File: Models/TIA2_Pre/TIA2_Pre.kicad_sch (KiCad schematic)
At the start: 0 parts

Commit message: Save progress
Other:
- note added: "Input: 2.5V power Input: -1.5V power Input: current Output: pre voltage Ground connection(s) not yet elaborated"
- note removed: "Input: 2.5V power (grounded interconnect) Input: -1.5V power (grounded interconnect) Input: current Output: voltage (grounded interconnect)"
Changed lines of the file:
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@@
 	(generator_version "9.0")
 	(paper "A4")
-	(text "Input: 2.5V power (grounded interconnect)\nInput: -1.5V power (grounded interconnect)\nInput: current\nOutput: voltage (grounded interconnect)"
+	(text "Input: 2.5V power\nInput: -1.5V power\nInput: current\nOutput: pre voltage\n\nGround connection(s) not yet elaborated"
 		(exclude_from_sim no)
 		(at 158.242 76.962 0)

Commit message: Save progress
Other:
- note added: "Input: 2.5V power Input: -1.5V power Input: current Output: pre voltage Output: AD8615 output Ground connection(s) not yet elaborated"
- note removed: "Input: 2.5V power Input: -1.5V power Input: current Output: pre voltage Ground connection(s) not yet elaborated"
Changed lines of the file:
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@@
 	(generator_version "9.0")
 	(paper "A4")
-	(text "Input: 2.5V power\nInput: -1.5V power\nInput: current\nOutput: pre voltage\n\nGround connection(s) not yet elaborated"
+	(text "Input: 2.5V power\nInput: -1.5V power\nInput: current\nOutput: pre voltage\nOutput: AD8615 output\n\nGround connection(s) not yet elaborated"
 		(exclude_from_sim no)
 		(at 158.242 76.962 0)

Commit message: Save progress
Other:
- note added: "Input: 2.5V power Input: -1.5V power Input: current Output: pre voltage Output: AD8615 output"
- note removed: "Input: 2.5V power Input: -1.5V power Input: current Output: pre voltage Output: AD8615 output Ground connection(s) not yet elaborated"
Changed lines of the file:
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@@
 	(generator_version "9.0")
 	(paper "A4")
-	(text "Input: 2.5V power\nInput: -1.5V power\nInput: current\nOutput: pre voltage\nOutput: AD8615 output\n\nGround connection(s) not yet elaborated"
+	(text "Input: 2.5V power\nInput: -1.5V power\nInput: current\nOutput: pre voltage\nOutput: AD8615 output"
 		(exclude_from_sim no)
 		(at 158.242 76.962 0)
@@
 	(sheet
 		(at 101.6 76.2)
-		(size 50.8 50.8)
+		(size 50.8 25.4)
 		(exclude_from_sim no)
 		(in_bom yes)
@@
 		)
 		(property "Sheetfile" "Amplifier.kicad_sch"
-			(at 101.6 127.5846 0)
+			(at 101.6 102.1846 0)
 			(effects
 				(font

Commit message: Save progress
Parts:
- added C3, C4: 1 uF, 0603, symbol Device:C
- added J3: Conn_01x03_Pin, symbol Connector:Conn_01x03_Pin
- added R1: 10, symbol Device:R_US
- added R3: 330M, 5%, 0603, symbol Device:R_US
- added U2: AD8615, symbol Amplifier_Operational:OP179GRT
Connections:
- new net: J3.1 (Pin_1), R1.1
- new net -1.5V: C4.1, U2.5 (V-)
- new net 2.5V: C3.1, U2.2 (V+)
- new net AD8615_Output: U2.1
- new net Current: R3.1, U2.4 (-)
- new net GND: C3.2, C4.2, J3.3 (Pin_3), R1.2
- new net ISO_GND: J3.2 (Pin_2), U2.3 (+)
- new net PreVoltage: R3.2
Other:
- removed sheet Amplifier
- note removed: "Input: 2.5V power Input: -1.5V power Input: current Output: pre voltage Output: AD8615 output"

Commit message: Save progress
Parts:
- R3: value 330M, 5%, 0603 -> 1G, 5%, 0603; Cost (none) -> $4.19; Purchase Link https://www.digikey.com/en/products/detail/vishay-dale/CRCW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 -> https://www.digikey.com/en/products/detail/stackpole-electr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
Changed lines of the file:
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@@
 			)
 		)
-		(property "Value" "330M, 5%, 0603"
+		(property "Value" "1G, 5%, 0603"
 			(at 135.89 95.25 90)
 			(effects
@@
 			)
 		)
-		(property "Purchase Link" "https://www.digikey.com/en/products/detail/vishay-dale/CRCW0603330MJPEAHR/5072104"
+		(property "Purchase Link" "https://www.digikey.com/en/products/detail/stackpole-electronics-inc/HVCB0603JDD1G00/5801231"
 			(at 135.89 99.06 0)
 			(effects
 				(font
+					(size 1.27 1.27)
+				)
+				(hide yes)
+			)
+		)
+		(property "Cost" "$4.19"
+			(at 135.89 99.06 90)
+			(effects
+				(font

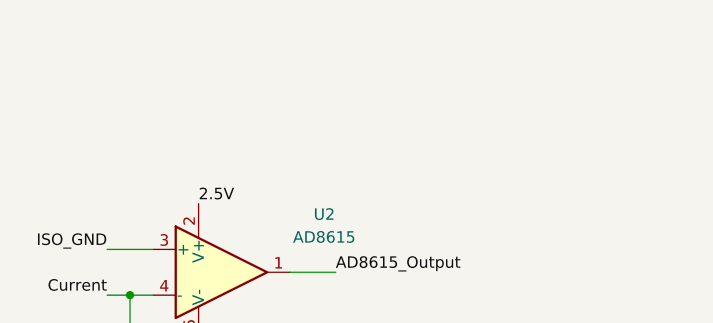
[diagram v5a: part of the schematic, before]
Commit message: Weird bug messes up FEM simulation results when I recompute objects in FreeCAD
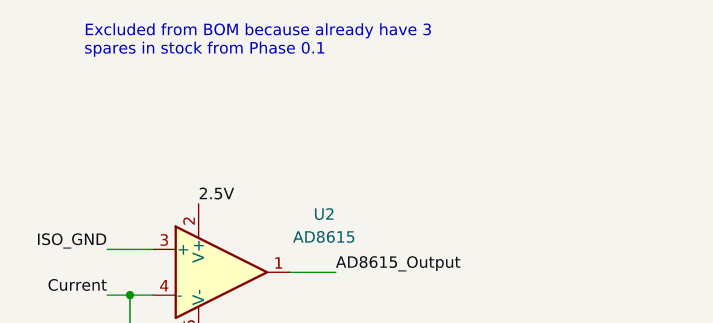
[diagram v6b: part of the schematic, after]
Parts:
- U2: now left out of the parts list
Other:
- note added: "Excluded from BOM because already have 3 spares in stock from Phase 0.1"
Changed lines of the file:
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@@
 	(generator_version "9.0")
 	(paper "A4")
+	(text "Excluded from BOM because already have 3\nspares in stock from Phase 0.1"
+		(exclude_from_sim no)
+		(at 121.92 46.228 0)
+		(effects
+			(font
+				(size 1.27 1.27)
+			)
+			(justify left top)
+		)
+	)
 	(junction
 		(at 127 76.2)
@@
 		(unit 1)
 		(exclude_from_sim no)
-		(in_bom yes)
+		(in_bom no)
 		(on_board yes)
 		(dnp no)

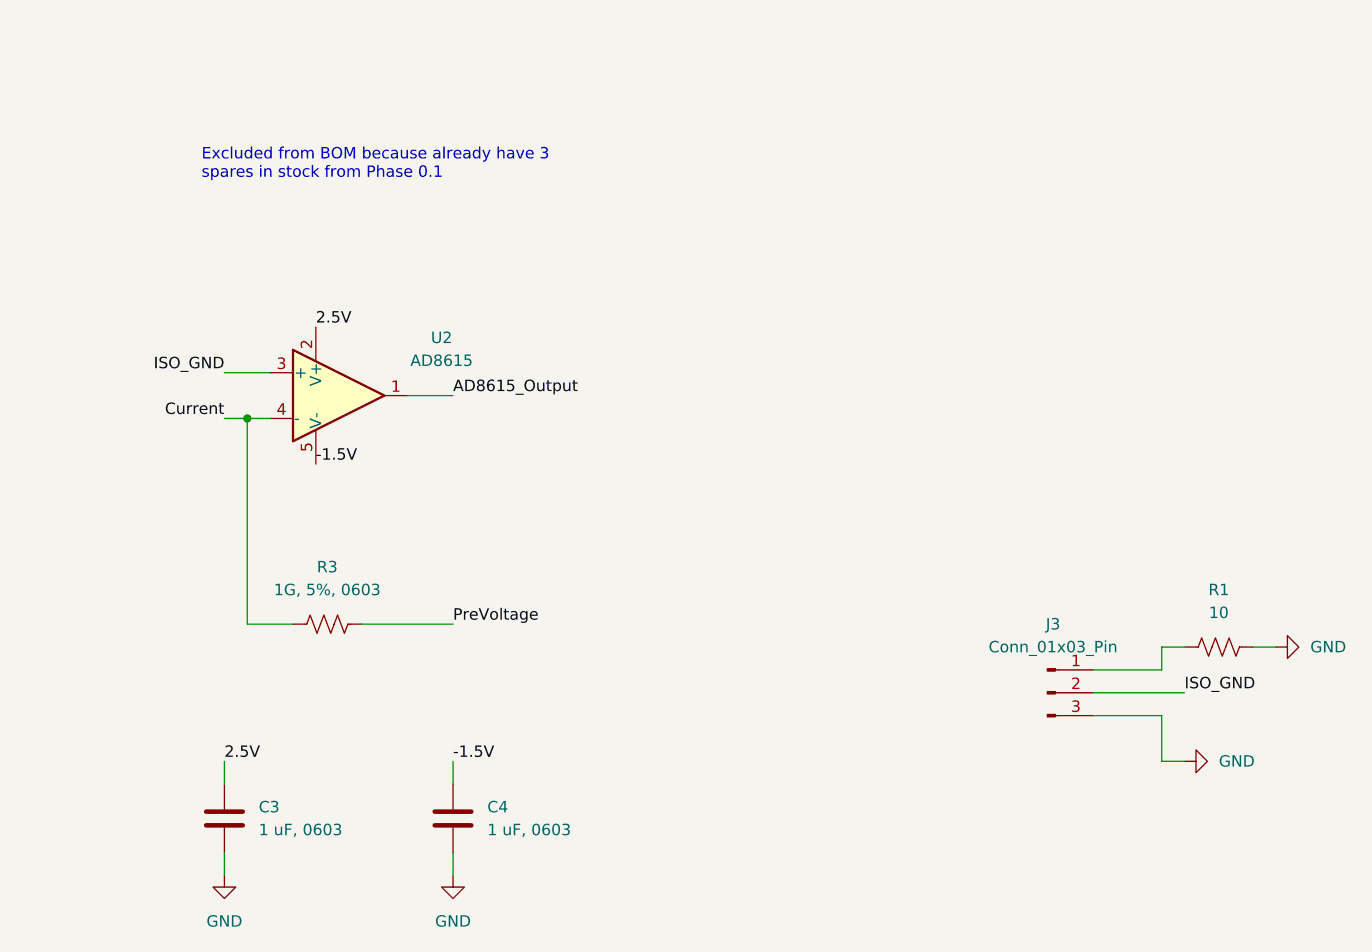
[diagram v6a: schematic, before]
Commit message: ERC passes for the two new boards
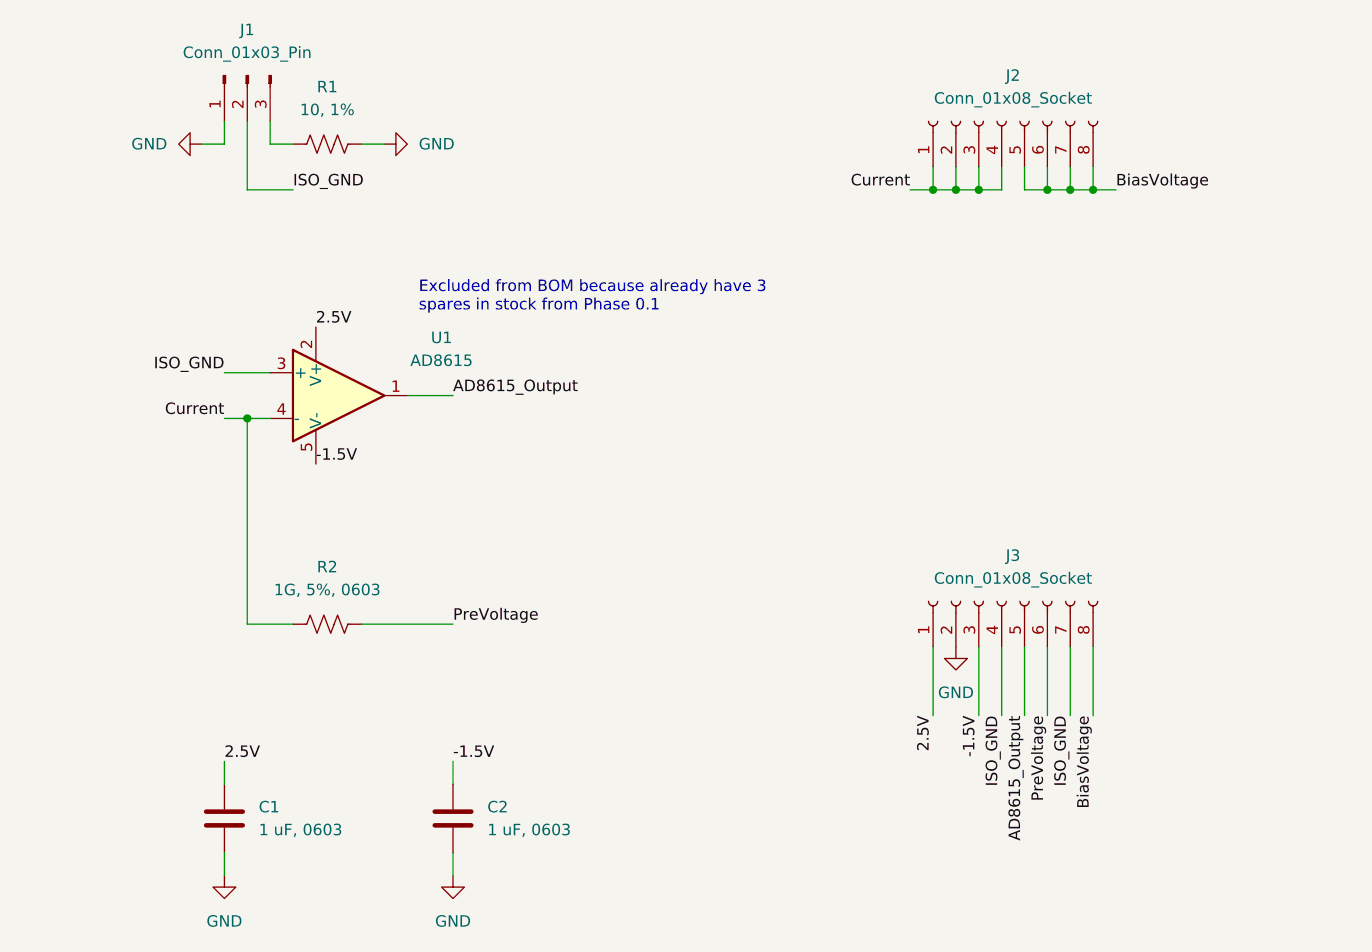
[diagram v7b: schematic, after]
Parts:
- removed J3: Conn_01x03_Pin, symbol Connector:Conn_01x03_Pin
- added J1: Conn_01x03_Pin, Connector_Custom:PinHeader_1x3, symbol Connector:Conn_01x03_Pin
- added J2, J3: Conn_01x08_Socket, Connector_Custom:PinSocket_1x8, symbol Connector:Conn_01x08_Socket
- C1: renamed from C3; footprint (none) -> TwoTerminal:CAPC0603; Cost (none) -> $0.078; Purchase Link (none) -> https://www.digikey.com/en/products/detail/murata-electroni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
- C2: renamed from C4; footprint (none) -> TwoTerminal:CAPC0603; Cost (none) -> $0.078; Purchase Link (none) -> https://www.digikey.com/en/products/detail/murata-electroni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
- R1: value 10 -> 10, 1%; footprint (none) -> TwoTerminal:RESC0603; Cost (none) -> $0.030; Purchase Link (none) -> https://www.digikey.com/en/products/detail/vishay-dale/CRCW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
- R2: renamed from R3; footprint (none) -> TwoTerminal:RESC0603
- U1: renamed from U2; footprint (none) -> IC:AD8615
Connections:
- net -1.5V: now also J3.3 (Pin_3)
- net 2.5V: now also J3.1 (Pin_1)
- net AD8615_Output: now also J3.5 (Pin_5)
- net Current: now also J2.1 (Pin_1), J2.2 (Pin_2), J2.3 (Pin_3), J2.4 (Pin_4)
- net GND: now also J1.1 (Pin_1), J3.2 (Pin_2)
- net ISO_GND: now also J1.2 (Pin_2), J3.4 (Pin_4), J3.7 (Pin_7)
- net PreVoltage: now also J3.6 (Pin_6)
- net at R1.1: now also J1.3 (Pin_3)
- new net BiasVoltage: J2.5 (Pin_5), J2.6 (Pin_6), J2.7 (Pin_7), J2.8 (Pin_8), J3.8 (Pin_8)

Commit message: First time that all PCBs are fully wired
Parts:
- removed J3: Conn_01x08_Socket, Connector_Custom:PinSocket_1x8, symbol Connector:Conn_01x08_Socket
- added J2: Conn_01x04_Socket, Connector_Custom:PinSocket_1x4, symbol Connector:Conn_01x04_Socket
- added J4: Conn_01x05_Socket, Connector_Custom:PinSocket_1x5, symbol Connector:Conn_01x05_Socket
- U1: symbol Amplifier_Operational:OP179GRT -> Vendor:AD8615; now in the parts list
- renumbered J2 to J3
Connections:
- net -1.5V: now also U1.2 (V-), J2.3 (Pin_3); no longer U1.5 (V-)
- net 2.5V: now also U1.5 (V+), J2.1 (Pin_1); no longer U1.2 (V+)
- net AD8615_Output: now also J4.2 (Pin_2)
- net BiasVoltage: now also J4.5 (Pin_5)
- net GND: now also J2.2 (Pin_2), J2.4 (Pin_4)
- net ISO_GND: now also J4.1 (Pin_1), J4.4 (Pin_4)
- net PreVoltage: now also J4.3 (Pin_3)
